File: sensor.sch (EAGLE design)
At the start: 16 parts

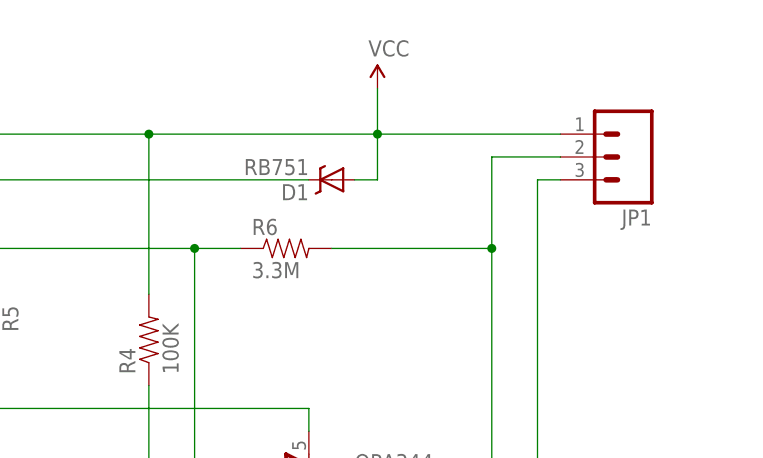
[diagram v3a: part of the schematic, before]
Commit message: sensor: update lbr and correct design
1. Add a reverse mount led.
2. Update output pad.
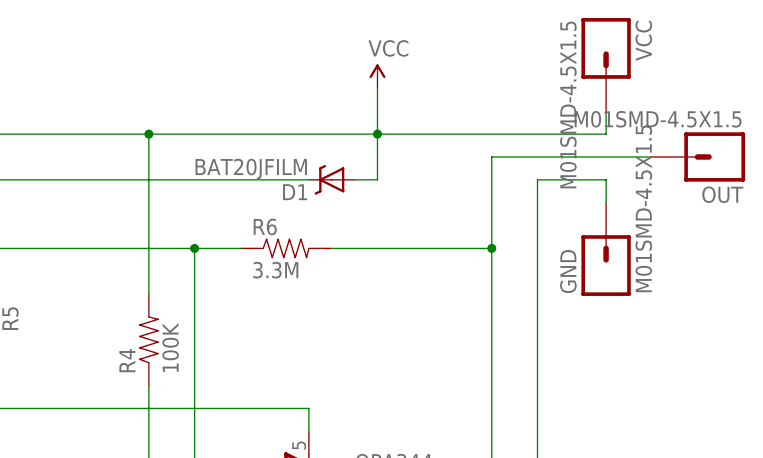
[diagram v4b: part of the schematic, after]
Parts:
- removed JP1: (no value), SparkFun-Connectors:M03LONGPADS
- added GND, OUT, VCC: M01SMD-4.5X1.5, SparkFun-Connectors:M01SMD-4.5X1.5
- D1: value RB751 -> BAT20JFILM; device SparkFun-DiscreteSemi:RB751 -> SparkFun-DiscreteSemi:BAT20JFILM
- LED1: device SparkFun-LED:LED0603 -> librae:LED
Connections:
- net GND: now also GND.1; no longer JP1.3
- net OUT: now also OUT.1; no longer JP1.2
- net VCC: now also VCC.1; no longer JP1.1
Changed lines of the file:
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@@
 <setting verticaltext="up"/>
 </settings>
-<grid distance="0.1" unitdist="inch" unit="inch" style="lines" multiple="1" display="no" altdistance="0.01" altunitdist="inch" altunit="inch"/>
+<grid distance="0.1" unitdist="inch" unit="inch" style="lines" multiple="1" display="yes" altdistance="0.01" altunitdist="inch" altunit="inch"/>
 <layers>
-<layer number="1" name="Top" color="4" fill="1" visible="no" active="no"/>
-<layer number="16" name="Bottom" color="1" fill="1" visible="no" active="no"/>
-<layer number="17" name="Pads" color="2" fill="1" visible="no" active="no"/>
-<layer number="18" name="Vias" color="2" fill="1" visible="no" active="no"/>
-<layer number="19" name="Unrouted" color="6" fill="1" visible="no" active="no"/>
-<layer number="20" name="Dimension" color="15" fill="1" visible="no" active="no"/>
-<layer number="21" name="tPlace" color="7" fill="1" visible="no" active="no"/>
-<layer number="22" name="bPlace" color="7" fill="1" visible="no" active="no"/>
-<layer number="23" name="tOrigins" color="15" fill="1" visible="no" active="no"/>
-<layer number="24" name="bOrigins" color="15" fill="1" visible="no" active="no"/>
-<layer number="25" name="tNames" color="7" fill="1" visible="no" active="no"/>
-<layer number="26" name="bNames" color="7" fill="1" visible="no" active="no"/>
-<layer number="27" name="tValues" color="7" fill="1" visible="no" active="no"/>
-<layer number="28" name="bValues" color="7" fill="1" visible="no" active="no"/>
+<layer number="1" name="Top" color="4" fill="1" visible="yes" active="no"/>
+<layer number="16" name="Bottom" color="1" fill="1" visible="yes" active="no"/>
+<layer number="17" name="Pads" color="2" fill="1" visible="yes" active="no"/>
+<layer number="18" name="Vias" color="2" fill="1" visible="yes" active="no"/>
+<layer number="19" name="Unrouted" color="6" fill="1" visible="yes" active="no"/>
+<layer number="20" name="Dimension" color="15" fill="1" visible="yes" active="no"/>
+<layer number="21" name="tPlace" color="7" fill="1" visible="yes" active="no"/>
+<layer number="22" name="bPlace" color="7" fill="1" visible="yes" active="no"/>
+<layer number="23" name="tOrigins" color="15" fill="1" visible="yes" active="no"/>
+<layer number="24" name="bOrigins" color="15" fill="1" visible="yes" active="no"/>
+<layer number="25" name="tNames" color="7" fill="1" visible="yes" active="no"/>
+<layer number="26" name="bNames" color="7" fill="1" visible="yes" active="no"/>
+<layer number="27" name="tValues" color="7" fill="1" visible="yes" active="no"/>
+<layer number="28" name="bValues" color="7" fill="1" visible="yes" active="no"/>
 <layer number="29" name="tStop" color="7" fill="3" visible="no" active="no"/>
 <layer number="30" name="bStop" color="7" fill="6" visible="no" active="no"/>
@@
 <layer number="35" name="tGlue" color="7" fill="4" visible="no" active="no"/>
 <layer number="36" name="bGlue" color="7" fill="5" visible="no" active="no"/>
-<layer number="37" name="tTest" color="7" fill="1" visible="no" active="no"/>
-<layer number="38" name="bTest" color="7" fill="1" visible="no" active="no"/>
+<layer number="37" name="tTest" color="7" fill="1" visible="yes" active="no"/>
+<layer number="38" name="bTest" color="7" fill="1" visible="yes" active="no"/>
 <layer number="39" name="tKeepout" color="4" fill="11" visible="no" active="no"/>
 <layer number="40" name="bKeepout" color="1" fill="11" visible="no" active="no"/>
@@
 <layer number="44" name="Drills" color="7" fill="1" visible="no" active="no"/>
 <layer number="45" name="Holes" color="7" fill="1" visible="no" active="no"/>
-<layer number="46" name="Milling" color="3" fill="1" visible="no" active="no"/>
-<layer number="47" name="Measures" color="7" fill="1" visible="no" active="no"/>
-<layer number="48" name="Document" color="7" fill="1" visible="no" active="no"/>
-<layer number="49" name="Reference" color="7" fill="1" visible="no" active="no"/>
-<layer number="50" name="dxf" color="7" fill="1" visible="no" active="no"/>
-<layer number="51" name="tDocu" color="7" fill="1" visible="no" active="no"/>
-<layer number="52" name="bDocu" color="7" fill="1" visible="no" active="no"/>
-<layer number="53" name="tGND_GNDA" color="7" fill="9" visible="no" active="no"/>
-<layer number="54" name="bGND_GNDA" color="1" fill="9" visible="no" active="no"/>
-<layer number="56" name="wert" color="7" fill="1" visible="no" active="no"/>
+<layer number="46" name="Milling" color="3" fill="1" visible="yes" active="no"/>
+<layer number="47" name="Measures" color="7" fill="1" visible="yes" active="no"/>
+<layer number="48" name="Document" color="7" fill="1" visible="yes" active="no"/>
+<layer number="49" name="Reference" color="7" fill="1" visible="yes" active="no"/>
+<layer number="50" name="dxf" color="7" fill="1" visible="yes" active="no"/>
+<layer number="51" name="tDocu" color="7" fill="1" visible="yes" active="no"/>
+<layer number="52" name="bDocu" color="7" fill="1" visible="yes" active="no"/>
+<layer number="53" name="tGND_GNDA" color="7" fill="9" visible="yes" active="no"/>
+<layer number="54" name="bGND_GNDA" color="1" fill="9" visible="yes" active="no"/>
+<layer number="56" name="wert" color="7" fill="1" visible="yes" active="no"/>
 <layer number="91" name="Nets" color="2" fill="1" visible="yes" active="yes"/>
 <layer number="92" name="Busses" color="1" fill="1" visible="yes" active="yes"/>
@@
 <attribute name="VALUE" value="10K"/>
 </part>
-<part name="JP1" library="SparkFun-Connectors" deviceset="M03" device="LONGPADS"/>
-<part name="LED1" library="SparkFun-LED" deviceset="LED" device="0603"/>
 <part name="GND1" library="SparkFun-Aesthetics" deviceset="GND" device=""/>
 <part name="SUPPLY1" library="SparkFun-Aesthetics" deviceset="VCC" device=""/>
 <part name="APDS1" library="librae" deviceset="APDS-9008" device=""/>
-<part name="D1" library="SparkFun-DiscreteSemi" deviceset="RB751" device="" value="RB751"/>
+<part name="LED1" library="librae" deviceset="LED" device=""/>
+<part name="D1" library="SparkFun-DiscreteSemi" deviceset="BAT20JFILM" device="" value="BAT20JFILM"/>
+<part name="VCC" library="SparkFun-Connectors" deviceset="M01" device="SMD-4.5X1.5" value="M01SMD-4.5X1.5"/>
+<part name="OUT" library="SparkFun-Connectors" deviceset="M01" device="SMD-4.5X1.5" value="M01SMD-4.5X1.5"/>
+<part name="GND" library="SparkFun-Connectors" deviceset="M01" device="SMD-4.5X1.5" value="M01SMD-4.5X1.5"/>
 </parts>
 <sheets>
@@
 <instance part="R5" gate="G$1" x="10.16" y="27.94" rot="R270"/>
 <instance part="R6" gate="G$1" x="43.18" y="38.1"/>
-<instance part="JP1" gate="G$1" x="81.28" y="48.26" rot="R180"/>
-<instance part="LED1" gate="G$1" x="-60.96" y="30.48"/>
 <instance part="GND1" gate="1" x="-7.62" y="-22.86"/>
 <instance part="SUPPLY1" gate="1" x="53.34" y="55.88"/>
 <instance part="APDS1" gate="G$1" x="-43.18" y="12.7" rot="R90"/>
+<instance part="LED1" gate="G$1" x="-60.96" y="30.48"/>
 <instance part="D1" gate="G$1" x="48.26" y="45.72" rot="R180"/>
+<instance part="VCC" gate="G$1" x="78.74" y="60.96" rot="R270"/>
+<instance part="OUT" gate="G$1" x="91.44" y="48.26" rot="R180"/>
+<instance part="GND" gate="G$1" x="78.74" y="35.56" rot="R90"/>
 </instances>
 <busses>
@@
 <net name="VCC" class="0">
 <segment>
-<pinref part="JP1" gate="G$1" pin="1"/>
-<wire x1="73.66" y1="50.8" x2="53.34" y2="50.8" width="0.1524" layer="91"/>
+<wire x1="78.74" y1="50.8" x2="53.34" y2="50.8" width="0.1524" layer="91"/>
 <pinref part="C5" gate="G$1" pin="1"/>
 <wire x1="53.34" y1="50.8" x2="27.94" y2="50.8" width="0.1524" layer="91"/>
@@
 <wire x1="53.34" y1="45.72" x2="53.34" y2="50.8" width="0.1524" layer="91"/>
 <junction x="53.34" y="50.8"/>
-<pinref part="LED1" gate="G$1" pin="A"/>
 <wire x1="-60.96" y1="33.02" x2="-60.96" y2="50.8" width="0.1524" layer="91"/>
 <junction x="-60.96" y="50.8"/>
@@
 <pinref part="SUPPLY1" gate="1" pin="VCC"/>
 <wire x1="53.34" y1="50.8" x2="53.34" y2="55.88" width="0.1524" layer="91"/>
+<pinref part="LED1" gate="G$1" pin="A"/>
 <pinref part="D1" gate="G$1" pin="A"/>
+<pinref part="VCC" gate="G$1" pin="1"/>
+<wire x1="78.74" y1="50.8" x2="78.74" y2="53.34" width="0.1524" layer="91"/>
 </segment>
 </net>
@@
 <net name="OUT" class="0">
 <segment>
-<pinref part="JP1" gate="G$1" pin="2"/>
-<wire x1="73.66" y1="48.26" x2="66.04" y2="48.26" width="0.1524" layer="91"/>
 <wire x1="66.04" y1="48.26" x2="66.04" y2="38.1" width="0.1524" layer="91"/>
 <pinref part="MCP6001" gate="G$1" pin="OUT"/>
@@
 <wire x1="48.26" y1="38.1" x2="66.04" y2="38.1" width="0.1524" layer="91"/>
 <junction x="66.04" y="38.1"/>
+<pinref part="OUT" gate="G$1" pin="1"/>
+<wire x1="66.04" y1="48.26" x2="83.82" y2="48.26" width="0.1524" layer="91"/>
 </segment>
 </net>
 <net name="N$3" class="0">
 <segment>
-<pinref part="LED1" gate="G$1" pin="C"/>
 <pinref part="R1" gate="G$1" pin="2"/>
 <wire x1="-60.96" y1="25.4" x2="-60.96" y2="5.08" width="0.1524" layer="91"/>
+<pinref part="LED1" gate="G$1" pin="C"/>
 </segment>
 </net>
@@
 <pinref part="GND1" gate="1" pin="GND"/>
 <wire x1="-7.62" y1="-20.32" x2="-7.62" y2="-17.78" width="0.1524" layer="91"/>
-<pinref part="JP1" gate="G$1" pin="3"/>
-<wire x1="73.66" y1="45.72" x2="71.12" y2="45.72" width="0.1524" layer="91"/>
 <wire x1="71.12" y1="45.72" x2="71.12" y2="-17.78" width="0.1524" layer="91"/>
 <wire x1="71.12" y1="-17.78" x2="45.72" y2="-17.78" width="0.1524" layer="91"/>
@@
 <wire x1="-33.02" y1="2.54" x2="-33.02" y2="-17.78" width="0.1524" layer="91"/>
 <junction x="-33.02" y="-17.78"/>
-</segment>
-</net>
+<pinref part="GND" gate="G$1" pin="1"/>
+<wire x1="71.12" y1="45.72" x2="78.74" y2="45.72" width="0.1524" layer="91"/>
+<wire x1="78.74" y1="45.72" x2="78.74" y2="43.18" width="0.1524" layer="91"/>
+</segment>
+</net>
